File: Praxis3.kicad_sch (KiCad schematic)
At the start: 6 parts, among them Q1 2SC4213, Q2 2N7002, U1 LM555xM, U2 TPL5010, U5 ATmega16M1-A

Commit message: improved
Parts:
- removed D10: LED, LED_SMD:LED_PLCC-2_3x2mm_KA, symbol Device:LED
- removed Q2: 2N7002, Package_TO_SOT_SMD:SOT-23, symbol Transistor_FET:2N7002
- added S60: MSS6-V-T_R, NiksKiCadLibrary:MSS6VTR, symbol NiksKiCadLibrary:MSS6-V-T_R
- added SW60: MSS3-V-T/R, NiksKiCadLibrary:MSS3VTR, symbol NiksKiCadLibrary:MSS3-V-T_R
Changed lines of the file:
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@@
 (kicad_sch (version 20230121) (generator eeschema)
   (paper "A4")
-  (wire (pts (xy 138.43 50.8) (xy 138.43 44.45))
-    (stroke (width 0) (type default))
-  )
   (text "SN74LVC2G08DCUR" (at 128.27 71.12 0)
     (effects (font (size 1.27 1.27)) (justify left bottom))
@@
     (effects (font (size 1.27 1.27)) (justify left bottom))
   )
-  (symbol (lib_id "Transistor_FET:2N7002") (at 162.56 64.77 0) (unit 1)
-    (in_bom yes) (on_board yes) (dnp no) (fields_autoplaced)
-    (property "Reference" "Q2" (at 168.91 63.5 0)
-      (effects (font (size 1.27 1.27)) (justify left))
-    )
-    (property "Value" "2N7002" (at 168.91 66.04 0)
-      (effects (font (size 1.27 1.27)) (justify left))
-    )
-    (property "Footprint" "Package_TO_SOT_SMD:SOT-23" (at 167.64 66.675 0)
-      (effects (font (size 1.27 1.27) italic) (justify left) hide)
-    )
-    (property "Datasheet" "https://www.onsemi.com/pub/Collateral/NDS7002A-D.PDF" (at 162.56 64.77 0)
-      (effects (font (size 1.27 1.27)) (justify left) hide)
-    )
-    (property "Manufacturer Part Number" "2N7002H6327XTSA2" (at 162.56 64.77 0)
-      (effects (font (size 1.27 1.27)) hide)
-    )
-    (property "Supplier Part Number" "2443474" (at 162.56 64.77 0)
-      (effects (font (size 1.27 1.27)) hide)
-    )
-    (property "Supplier" "Farnell" (at 162.56 64.77 0)
-      (effects (font (size 1.27 1.27)) hide)
-    )
-    (pin "1")
-    (pin "2")
-    (pin "3")
-    (instances
-      (project "FLW_EkGk_Handlöten_PCB1"
-        (path "/db211800-561f-4a5f-a2c7-7ea3433d307f"
-          (reference "Q2") (unit 1)
-        )
-        (path "/db211800-561f-4a5f-a2c7-7ea3433d307f/5715bbb9-a5c5-4f42-9ee1-fed89f2d507d"
-          (reference "Q2") (unit 1)
-        )
-      )
-    )
-  )
-  (symbol (lib_id "Device:LED") (at 138.43 40.64 90) (unit 1)
-    (in_bom yes) (on_board yes) (dnp no) (fields_autoplaced)
-    (property "Reference" "D10" (at 135.89 43.4975 90)
-      (effects (font (size 1.27 1.27)) (justify left))
-    )
-    (property "Value" "LED" (at 135.89 40.9575 90)
-      (effects (font (size 1.27 1.27)) (justify left))
-    )
-    (property "Footprint" "LED_SMD:LED_PLCC-2_3x2mm_KA" (at 138.43 40.64 0)
-      (effects (font (size 1.27 1.27)) hide)
-    )
-    (property "Datasheet" "~" (at 138.43 40.64 0)
-      (effects (font (size 1.27 1.27)) hide)
-    )
-    (pin "1")
-    (pin "2")
-    (instances
-      (project "FLW_EkGk_Handlöten_PCB1"
-        (path "/db211800-561f-4a5f-a2c7-7ea3433d307f"
-          (reference "D10") (unit 1)
-        )
-        (path "/db211800-561f-4a5f-a2c7-7ea3433d307f/5715bbb9-a5c5-4f42-9ee1-fed89f2d507d"
-          (reference "D9") (unit 1)
+  (symbol (lib_id "NiksKiCadLibrary:MSS3-V-T_R") (at 163.83 48.26 0) (unit 1)
+    (in_bom yes) (on_board yes) (dnp no) (fields_autoplaced)
+    (property "Reference" "SW60" (at 176.53 41.91 0)
+      (effects (font (size 1.524 1.524)))
+    )
+    (property "Value" "MSS3-V-T/R" (at 176.53 44.45 0)
+      (effects (font (size 1.524 1.524)))
+    )
+    (property "Footprint" "NiksKiCadLibrary:MSS3VTR" (at 163.83 48.26 0)
+      (effects (font (size 1.27 1.27) italic) hide)
+    )
+    (property "Datasheet" "MSS3-V-T/R" (at 163.83 48.26 0)
+      (effects (font (size 1.27 1.27) italic) hide)
+    )
+    (pin "1")
+    (pin "2")
+    (pin "3")
+    (instances
+      (project "FLW_EkGk_Handlöten_PCB1"
+        (path "/db211800-561f-4a5f-a2c7-7ea3433d307f/5715bbb9-a5c5-4f42-9ee1-fed89f2d507d"
+          (reference "SW60") (unit 1)
         )
       )
@@
     )
   )
-  (symbol (lib_id "power:GNDD") (at 138.43 50.8 0) (unit 1)
-    (in_bom yes) (on_board yes) (dnp no) (fields_autoplaced)
-    (property "Reference" "#PWR02" (at 138.43 57.15 0)
-      (effects (font (size 1.27 1.27)) hide)
-    )
-    (property "Value" "GNDD" (at 138.43 54.61 0)
-      (effects (font (size 1.27 1.27)))
-    )
-    (property "Footprint" "" (at 138.43 50.8 0)
-      (effects (font (size 1.27 1.27)) hide)
-    )
-    (property "Datasheet" "" (at 138.43 50.8 0)
-      (effects (font (size 1.27 1.27)) hide)
-    )
-    (pin "1")
-    (instances
-      (project "FLW_EkGk_Handlöten_PCB1"
-        (path "/db211800-561f-4a5f-a2c7-7ea3433d307f/5715bbb9-a5c5-4f42-9ee1-fed89f2d507d"
-          (reference "#PWR02") (unit 1)
-        )
-      )
-    )
-  )
   (symbol (lib_id "Timer:LM555xM") (at 149.86 135.89 0) (unit 1)
     (in_bom yes) (on_board yes) (dnp no) (fields_autoplaced)
@@
         )
       )
+    )
+  )
+  (symbol (lib_id "NiksKiCadLibrary:MSS6-V-T_R") (at 194.945 96.52 0) (unit 1)
+    (in_bom yes) (on_board yes) (dnp no) (fields_autoplaced)
+    (property "Reference" "S60" (at 222.885 90.8303 0)
+      (effects (font (size 1.27 1.27)))
+    )
+    (property "Value" "MSS6-V-T_R" (at 222.885 93.3703 0)
+      (effects (font (size 1.27 1.27)))
+    )
+    (property "Footprint" "NiksKiCadLibrary:MSS6VTR" (at 216.535 181.28 0)
+      (effects (font (size 1.27 1.27)) (justify left top) hide)
+    )
+    (property "Datasheet" "http://www.dip.com.tw/en/en-product-information/en-switch005/item/download/2644_d484074ddae8110c965b39aa743c4160" (at 216.535 281.28 0)
+      (effects (font (size 1.27 1.27)) (justify left top) hide)
+    )
+    (property "Height" "2.9" (at 216.535 481.28 0)
+      (effects (font (size 1.27 1.27)) (justify left top) hide)
+    )
+    (property "Mouser Part Number" "113-MSS6-V-T/R" (at 216.535 581.28 0)
+      (effects (font (size 1.27 1.27)) (justify left top) hide)
+    )
+    (property "Mouser Price/Stock" "https://www.mouser.co.uk/ProductDetail/Diptronics/MSS6-V-T-R?qs=gTYE2QTfZfT81btvsnXi7w%3D%3D" (at 216.535 681.28 0)
+      (effects (font (size 1.27 1.27)) (justify left top) hide)
+    )
+    (property "Manufacturer_Name" "Diptronics" (at 216.535 781.28 0)
+      (effects (font (size 1.27 1.27)) (justify left top) hide)
+    )
+    (property "Manufacturer_Part_Number" "MSS6-V-T/R" (at 216.535 881.28 0)
+      (effects (font (size 1.27 1.27)) (justify left top) hide)
+    )
+    (pin "A1")
+    (pin "B1")
+    (pin "C1")
+    (pin "D1")
+    (pin "E1")
+    (pin "F1")
+    (pin "MP1")
+    (pin "MP2")
+    (pin "MP3")
+    (pin "MP4")
+    (instances
+      (project "FLW_EkGk_Handlöten_PCB1"
+        (path "/db211800-561f-4a5f-a2c7-7ea3433d307f/5715bbb9-a5c5-4f42-9ee1-fed89f2d507d"
+          (reference "S60") (unit 1)
+        )
+      )

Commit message: Continued
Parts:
- removed Q1: 2SC4213, Package_TO_SOT_SMD:SOT-323_SC-70, symbol Transistor_BJT:2SC4213
- removed U1: LM555xM, Package_SO:SOIC-8_3.9x4.9mm_P1.27mm, symbol Timer:LM555xM
- removed U5: ATmega16M1-A, Package_QFP:TQFP-32_7x7mm_P0.8mm, symbol MCU_Microchip_ATmega:ATmega16M1-A
- added C60: 100n, Capacitor_SMD:C_1206_3216Metric, symbol Device:C
- added IC60, IC61: HCF4094YM013TR, NiksKiCadLibrary:SOIC-16-SOIC127P600X175-16N, symbol NiksKiCadLibrary:HCF4094YM013TR
- added R1: 10k, Resistor_SMD:R_1206_3216Metric, symbol Device:R
- added SW61: B3U-3100P, SW_B3U-3100P_OMR, symbol NiksKiCadLibrary:B3U-3100P
- added U60: LM555xM, Package_SO:SOIC-8_3.9x4.9mm_P1.27mm, symbol NiksKiCadLibrary:LM555xM
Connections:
- net +5V0: now reaches SW60.1
- net +5V0: now also SW60.3, R1.1
- new net: IC60.2 (DATA), U60.3 (Q)
- new net: IC60.9 (QS), IC61.2 (DATA)
- new net: C60.1, U60.5 (CV)
- new net GND: C60.2, IC60.8 (VSS), IC61.8 (VSS), SW61.1, U60.1 (GND)
- new net nRST: R1.2, SW61.2, U60.4 (R)
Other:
- note removed: "LEDs: ASMT-SWB5-NW703"
- note removed: "LM555CM/NOPB"
- note removed: "SN74LVC2G08DCUR"
- note removed: "TPL5010DDCT"
- moved on the sheet: U2

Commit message: continued
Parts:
- removed C60: 100n, Capacitor_SMD:C_1206_3216Metric, symbol Device:C
- removed S60: MSS6-V-T_R, NiksKiCadLibrary:MSS6VTR, symbol NiksKiCadLibrary:MSS6-V-T_R
- removed U2: TPL5010, Package_TO_SOT_SMD:SOT-23-6, symbol Timer:TPL5010
- removed U60: LM555xM, Package_SO:SOIC-8_3.9x4.9mm_P1.27mm, symbol NiksKiCadLibrary:LM555xM
- added C61, C62: 100n, Capacitor_SMD:C_1206_3216Metric, symbol Device:C
- added LED60, LED61, LED62, LED63 (x2), LED64, LED65: SML-LX1206SIC-TR, FabLabWintiLibrary:LED_SML-LX1206SIC-TR_LUM, symbol FabLabWintiLibrary:SML-LX1206SIC-TR
- added Q60, Q61, Q62, Q63 (x2), Q64, Q65: 2N7002, Package_TO_SOT_SMD:SOT-23, symbol Transistor_FET:2N7002
- added R21 (x7): R, Resistor_SMD:R_1206_3216Metric, symbol Device:R
- SW61: footprint SW_B3U-3100P_OMR -> NiksKiCadLibrary:SW_B3U-3100P_OMR
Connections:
- net +5V0: now also R21.1, R21.1, R21.1, R21.1, R21.1, R21.1, R21.1
- net GND: now also C61.2, C62.2, Q60.2 (S), Q61.2 (S), Q62.2 (S), Q63.2 (S), Q63.2 (S), Q64.2 (S), Q65.2 (S)
- net STROBE: now reaches IC60.1 (STROBE)
- net STROBE: now also IC61.1 (STROBE)
- net LED4: now reaches IC60.14 (Q5)
- net LED4: now also Q64.1 (G)
- net EN: now reaches IC60.15 (OUTPUT_ENABLE)
- net EN: now also IC61.15 (OUTPUT_ENABLE)
- net at IC60.16 (VDD): now also C61.1
- net DATA: now reaches IC60.2 (DATA)
- net CLK: now reaches IC60.3 (CLOCK)
- net CLK: now also IC61.3 (CLOCK)
- net LED0: now reaches IC60.4 (Q1)
- net LED0: now also Q60.1 (G)
- net LED1: now reaches IC60.5 (Q2)
- net LED1: now also Q61.1 (G)
- net LED2: now reaches IC60.6 (Q3)
- net LED2: now also Q62.1 (G)
- net LED3: now reaches IC60.7 (Q4)
- net LED3: now also Q63.1 (G)
- net LED14: now reaches IC61.12 (Q7)
- net LED14: now also Q65.1 (G)
- net at IC61.16 (VDD): now also C62.1
- new net: LED60.2, R21.2
- new net: LED63.1, Q63.3 (D) (x2)
- new net: LED63.2, R21.2 (x2)
- new net: LED64.1, Q64.3 (D)
- new net: LED65.1, Q65.3 (D)
- new net: LED65.2, R21.2
- new net: LED64.2, R21.2
- new net: LED62.1, Q62.3 (D)
- new net: LED61.1, Q61.3 (D)
- new net: LED61.2, R21.2
- new net: LED60.1, Q60.3 (D)
- new net: LED62.2, R21.2
- new net LED15: Q63.1 (G)
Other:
- moved on the sheet: IC60, IC61, R1, SW60, SW61

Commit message: Almost finished
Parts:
- removed R1: 10k, Resistor_SMD:R_1206_3216Metric, symbol Device:R
- added R1 (x4): 10k, Resistor_SMD:R_1206_3216Metric, symbol Device:R
- added R1 (x2): 330R, Resistor_SMD:R_1206_3216Metric, symbol Device:R
- added SW62: B3U-3100P, SW_B3U-3100P_OMR, symbol NiksKiCadLibrary:B3U-3100P
- added TP60, TP61, TP62, TP63, TP64, TP65, TP66, TP67, TP68, TP69: TestPoint, NiksKiCadLibrary:TestPointSimpleSMD, symbol Connector:TestPoint
- SW61: footprint NiksKiCadLibrary:SW_B3U-3100P_OMR -> SW_B3U-3100P_OMR; Function (none) -> Manual Clock
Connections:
- net LED15 is gone; now on net led15: Q63.1 (G)
- net +5V0: now also SW60.B1 (2); no longer R21.1, R21.1, R21.1, R21.1, R21.1, R21.1, R21.1, SW60.1, SW60.3
- net CLK: now also R1.2, R1.2
- net DATA: now also R1.2, R1.2
- net EN: now also R1.2
- net GND: now also SW60.MP1 (4), SW60.MP2 (6), SW60.MP3 (5), SW60.MP4 (7), SW61.3 (BOSS), SW62.1, SW62.3 (BOSS)
- net STROBE: now also R1.2
- net at IC60.11 (Q8): now also TP61.1
- net at IC60.12 (Q7): now also TP60.1
- net led5: now reaches IC60.13 (Q6)
- net led5: now also Q65.1 (G)
- net +5v0: now reaches C61.1, IC60.16 (VDD)
- net +5v0: now also C62.1, IC61.16 (VDD), R21.1, R21.1, R21.1, R21.1, R21.1, R21.1, R21.1, SW60.A1 (1)
- net led15: now reaches IC61.11 (Q8)
- net at IC61.13 (Q6): now also TP67.1
- net at IC61.14 (Q5): now also TP66.1
- net at IC61.4 (Q1): now also TP62.1
- net at IC61.5 (Q2): now also TP63.1
- net at IC61.6 (Q3): now also TP64.1
- net at IC61.7 (Q4): now also TP65.1
- net at IC61.9 (QS): now also TP69.1
- net LED0 renamed led0
- net LED1 renamed led1
- net LED14: no longer names the net of IC61.12 (Q7)
- net LED14: now also TP68.1; no longer Q65.1 (G)
- net LED2 renamed led2
- net LED3 renamed led3
- net LED4 renamed led4
- net nRST: no longer names the net of SW61.2
- net nRST: now also R1.1
- new net: R1.1, SW62.2
- new net +3V3: R1.1, R1.1, R1.1, R1.1
- no-connect marks 0 -> 3
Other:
- note added: "..."
- moved on the sheet: C61, C62, IC60, IC61, LED60, LED61, LED62, LED63, LED64, LED65, Q60, Q61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

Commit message: Last changes
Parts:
- removed SW60: MSS3-V-T/R, NiksKiCadLibrary:MSS3VTR, symbol NiksKiCadLibrary:MSS3-V-T_R
- added SW60: MSS6-V-T_R, NiksKiCadLibrary:MSS6VTR, symbol NiksKiCadLibrary:MSS6-V-T_R
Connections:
- net +3V3: now also SW60.B1 (COM_1); no longer R1.1, R1.1, R1.1, R1.1
- net +5V0: now also SW60.E1 (COM_2)
- net +5v0: now also SW60.D1 (NO_2)
- net GND: now also SW60.MP1, SW60.MP2, SW60.MP3, SW60.MP4
- new net +3v3: R1.1, R1.1, R1.1, R1.1, SW60.A1 (NO_1)
- no-connect marks 3 -> 4

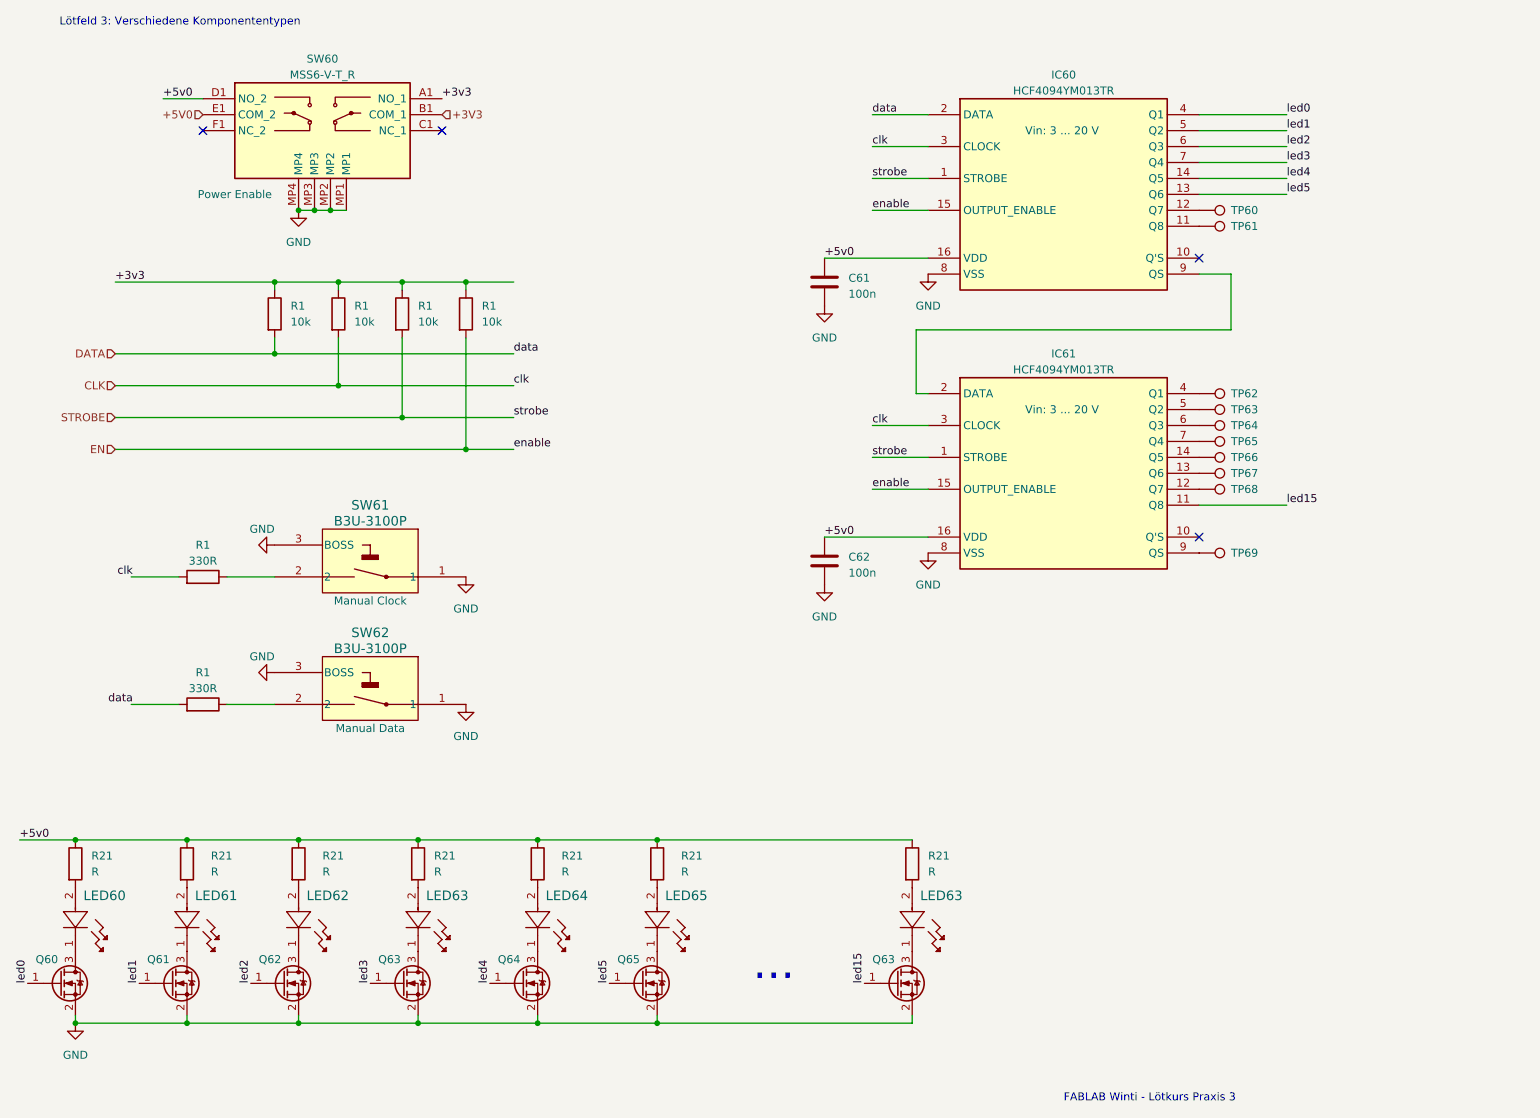
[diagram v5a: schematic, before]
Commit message: Resolves #2: Added current limiting resistor values (i.e. 620 Ohm)
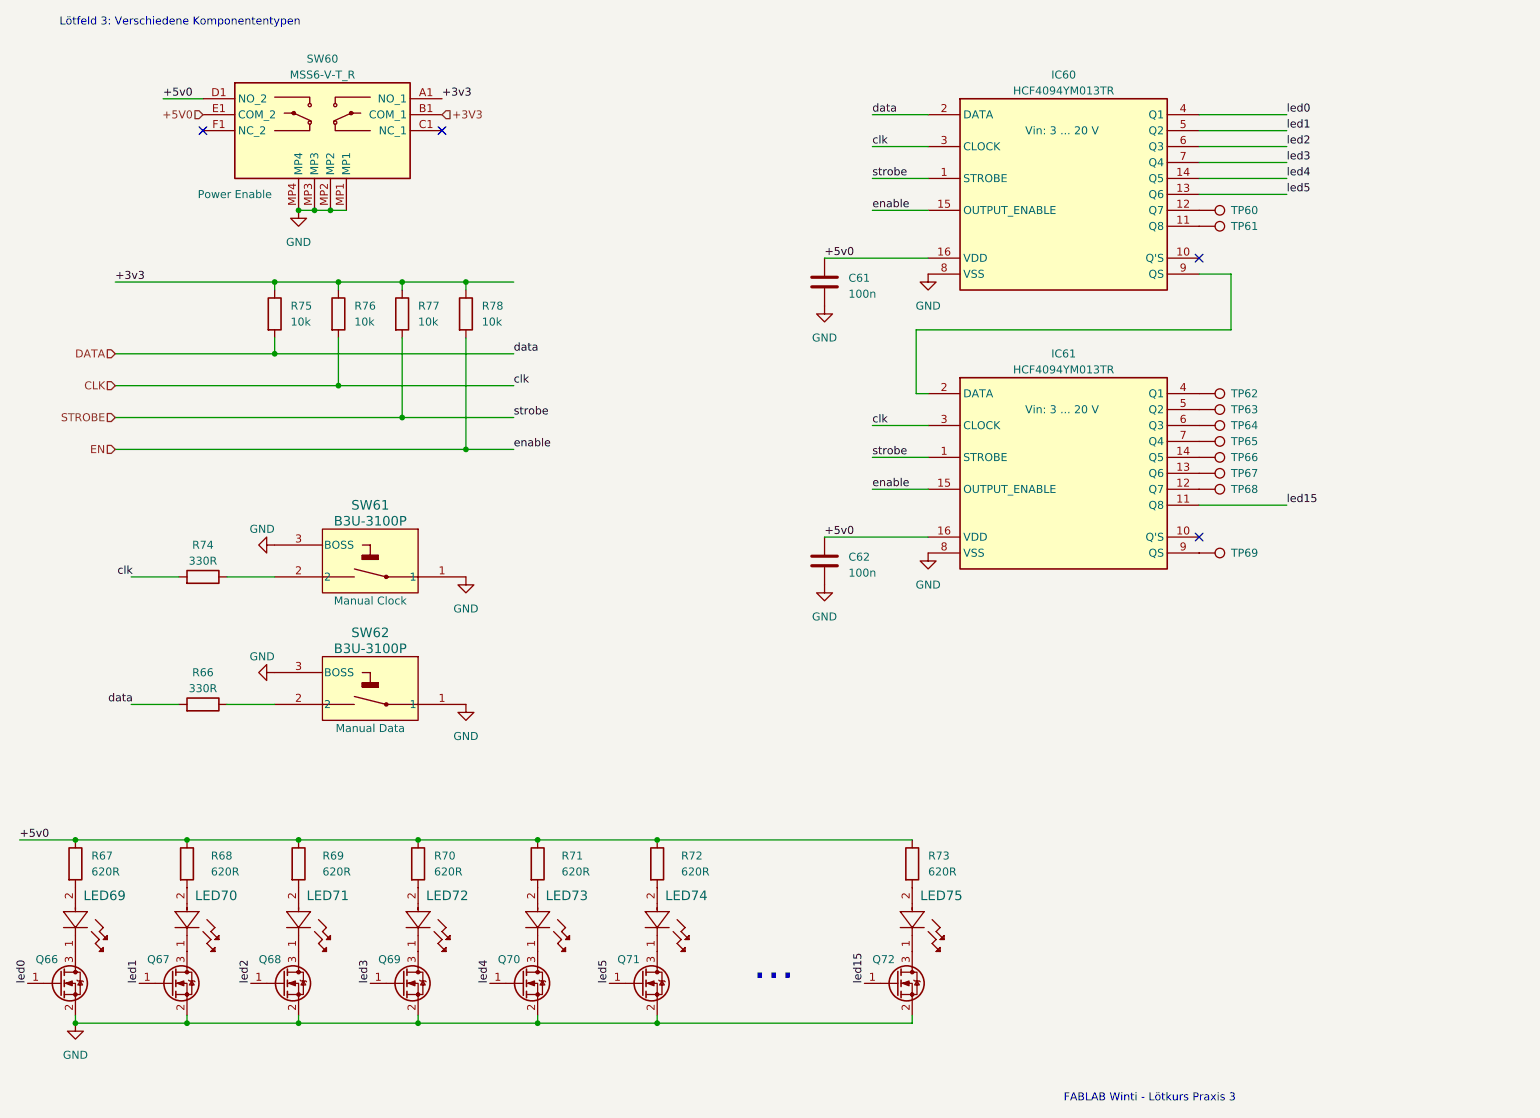
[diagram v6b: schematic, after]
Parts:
- R67, R68, R69, R70, R71, R72, R73: renamed from R21; value R -> 620R
- renumbered LED60 to LED69, LED61 to LED70, LED62 to LED71, LED63 to LED72, LED64 to LED73, LED65 to LED74, LED63 to LED75, Q60 to Q66, Q61 to Q67, Q62 to Q68, Q63 to Q69, Q64 to Q70, Q65 to Q71, Q63 to Q72, R1 to R66, R1 to R74, R1 to R75, R1 to R76, R1 to R77, R1 to R78
